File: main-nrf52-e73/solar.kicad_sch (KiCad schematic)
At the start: 13 parts, among them J2 Solar, J3 SOLARCURRENT, U4 BQ24210

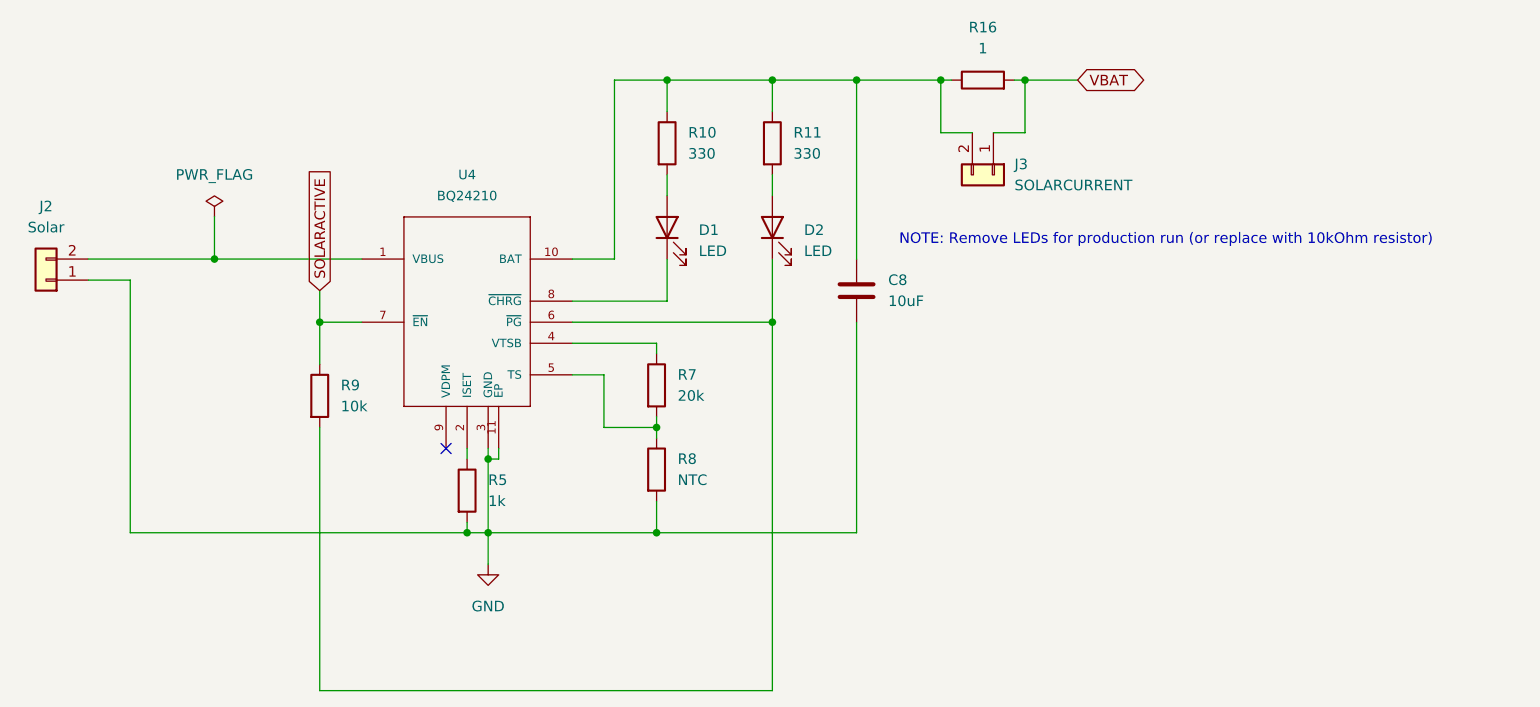
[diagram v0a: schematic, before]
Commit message: Finished first prototype of nRF52 powered main PCB.
Using Ebyte E73 module for the nRF chip.
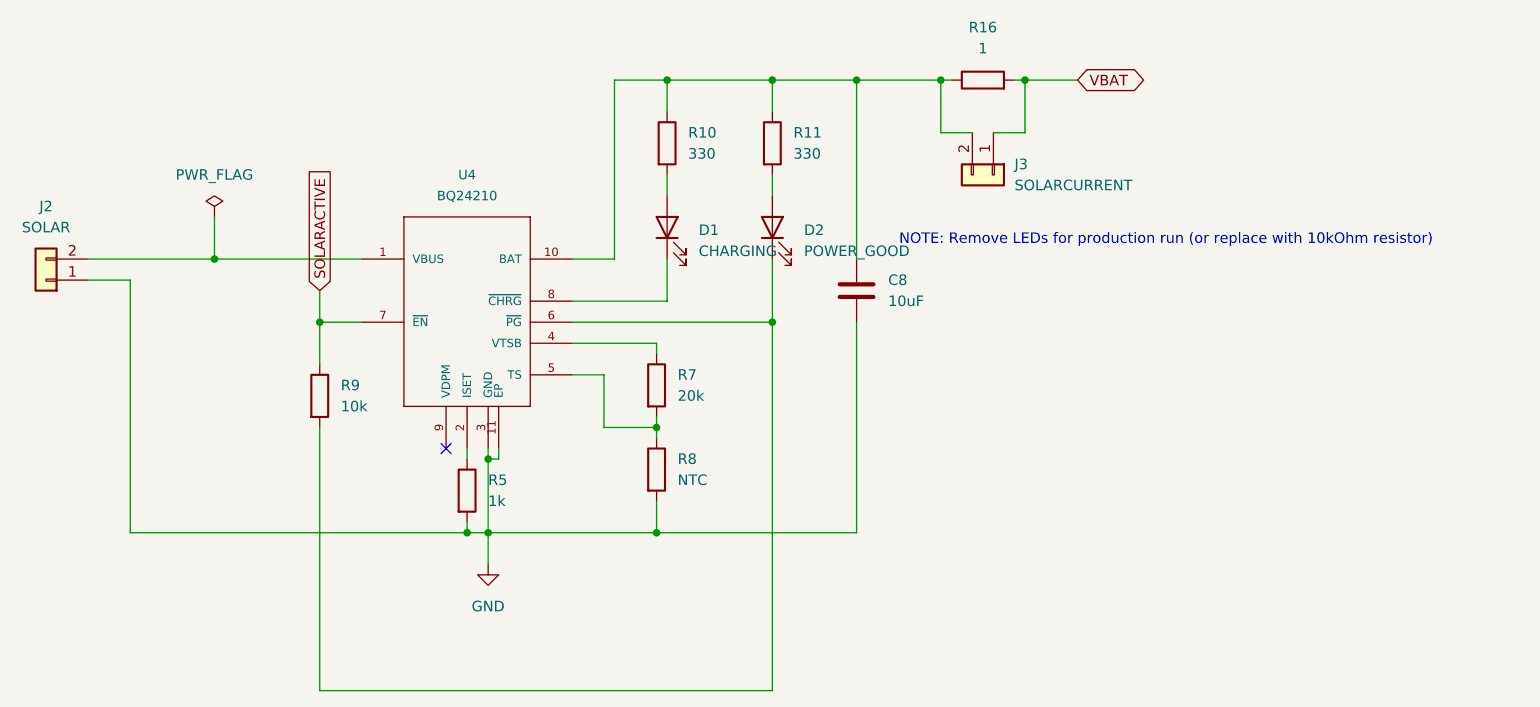
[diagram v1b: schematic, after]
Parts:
- C8: LCSC (none) -> C15850
- D1: value LED -> CHARGING; LCSC (none) -> C2286
- D2: value LED -> POWER_GOOD; LCSC (none) -> C2286
- J2: value Solar -> SOLAR
- R10, R11: LCSC (none) -> C23138
- R16: LCSC (none) -> C22936
- R5: LCSC (none) -> C21190
- R7: LCSC (none) -> C4184
- R8: LCSC (none) -> C76589
- R9: LCSC (none) -> C25804
- U4: LCSC (none) -> C524795
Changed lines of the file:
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@@
 			)
 		)
-		(property "Value" "LED"
+		(property "Value" "CHARGING"
 			(at 147.32 61.2774 90)
 			(effects
@@
 			)
 		)
+		(property "LCSC" "C2286"
+			(at 143.51 58.42 0)
+			(effects
+				(font
+					(size 1.27 1.27)
+				)
+				(hide yes)
+			)
+		)
 		(pin "1"
 		)
@@
 			)
 		)
+		(property "LCSC" "C4184"
+			(at 142.24 77.47 0)
+			(effects
+				(font
+					(size 1.27 1.27)
+				)
+				(hide yes)
+			)
+		)
 		(pin "1"
 		)
@@
 			)
 		)
+		(property "LCSC" ""
+			(at 182.88 52.07 0)
+			(effects
+				(font
+					(size 1.27 1.27)
+				)
+				(hide yes)
+			)
+		)
 		(pin "1"
 		)
@@
 			)
 		)
+		(property "LCSC" "C15850"
+			(at 166.37 66.04 0)
+			(effects
+				(font
+					(size 1.27 1.27)
+				)
+				(hide yes)
+			)
+		)
 		(pin "2"
 		)
@@
 			)
 		)
+		(property "LCSC" "C23138"
+			(at 143.51 48.26 0)
+			(effects
+				(font
+					(size 1.27 1.27)
+				)
+				(hide yes)
+			)
+		)
 		(pin "1"
 		)
@@
 			)
 		)
+		(property "LCSC" "C21190"
+			(at 119.38 90.17 0)
+			(effects
+				(font
+					(size 1.27 1.27)
+				)
+				(hide yes)
+			)
+		)
 		(pin "1"
 		)
@@
 			)
 		)
+		(property "LCSC" "C524795"
+			(at 119.38 67.31 0)
+			(effects
+				(font
+					(size 1.27 1.27)
+				)
+				(hide yes)
+			)
+		)
 		(pin "1"
 		)
@@
 			)
 		)
-		(property "Value" "Solar"
+		(property "Value" "SOLAR"
 			(at 68.58 58.42 0)
 			(effects
@@
 			)
 		)
+		(property "LCSC" ""
+			(at 68.58 64.77 0)
+			(effects
+				(font
+					(size 1.27 1.27)
+				)
+				(hide yes)
+			)
+		)
 		(pin "2"
 		)
@@
 			)
 		)
-		(property "Value" "LED"
+		(property "Value" "POWER_GOOD"
 			(at 160.02 61.2774 90)
 			(effects
@@
 			)
 		)
+		(property "LCSC" "C2286"
+			(at 156.21 58.42 0)
+			(effects
+				(font
+					(size 1.27 1.27)
+				)
+				(hide yes)
+			)
+		)
 		(pin "1"
 		)
@@
 			)
 		)
+		(property "LCSC" "C23138"
+			(at 156.21 48.26 0)
+			(effects
+				(font
+					(size 1.27 1.27)
+				)
+				(hide yes)
+			)
+		)
 		(pin "1"
 		)
@@
 			)
 		)
+		(property "LCSC" "C22936"
+			(at 181.61 40.64 0)
+			(effects
+				(font
+					(size 1.27 1.27)
+				)
+				(hide yes)
+			)
+		)
 		(pin "1"
 		)
@@
 			)
 		)
+		(property "LCSC" "C25804"
+			(at 101.6 78.74 0)
+			(effects
+				(font
+					(size 1.27 1.27)
+				)
+				(hide yes)
+			)
+		)
 		(pin "1"
 		)
@@
 			(at 142.24 87.63 0)
 			(effects
+				(font
+					(size 1.27 1.27)
+				)
+				(hide yes)
+			)
+		)
+		(property "LCSC" "C76589"
+			(at 142.24 87.63 0)
+			(effects
